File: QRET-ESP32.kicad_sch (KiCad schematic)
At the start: 3 parts

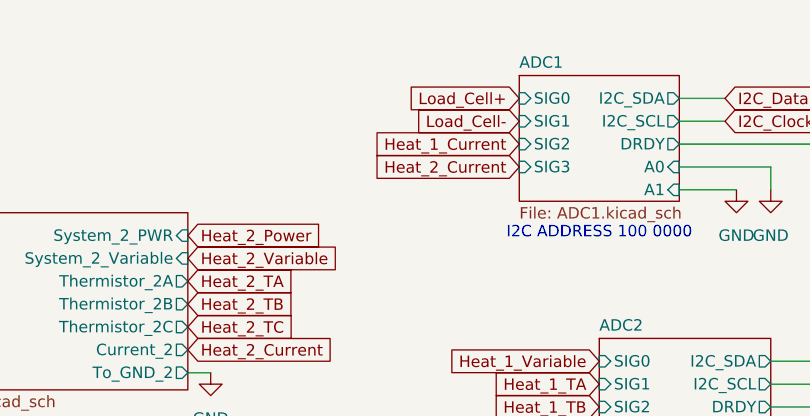
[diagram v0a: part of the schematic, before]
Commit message: Placed the general sets of components.
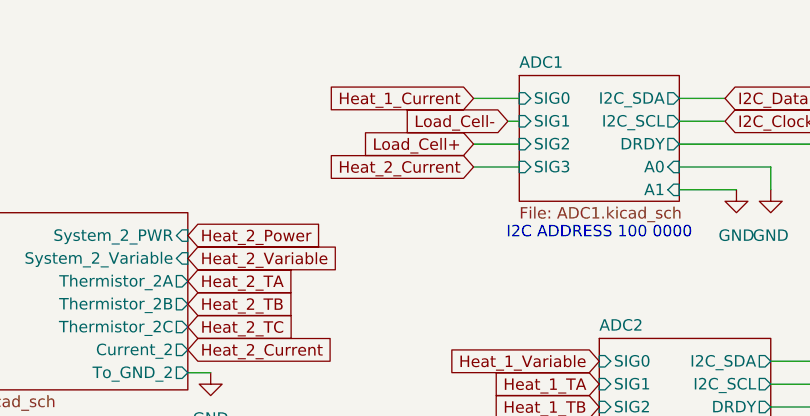
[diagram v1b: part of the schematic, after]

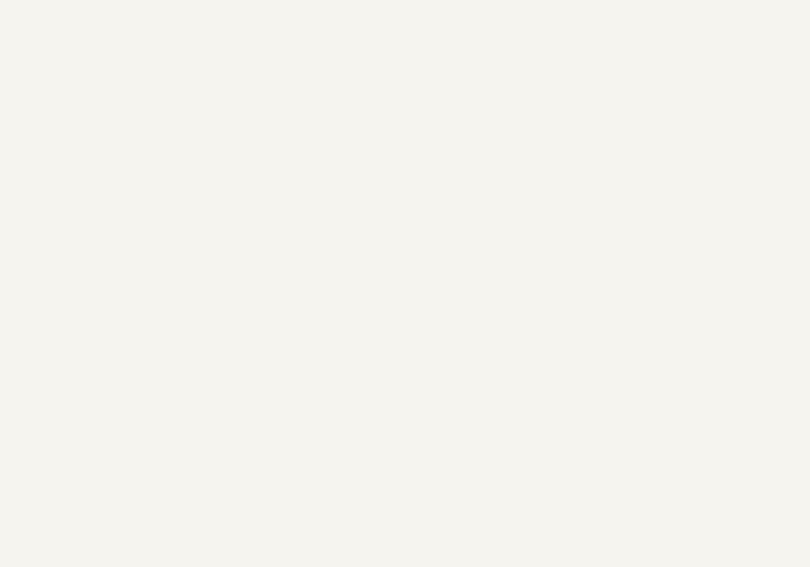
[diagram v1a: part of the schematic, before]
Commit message: General board shape, mounting holes, grounding plates.
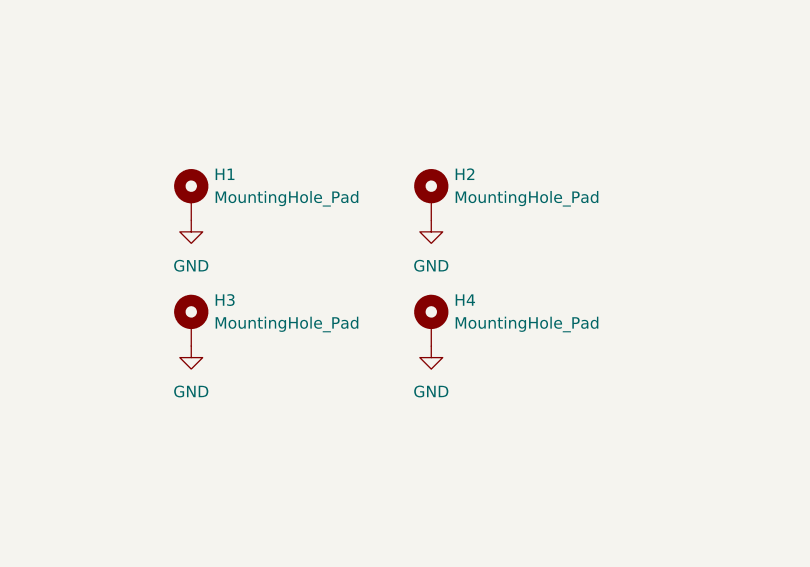
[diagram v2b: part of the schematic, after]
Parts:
- added H1, H2, H3, H4: MountingHole_Pad, MountingHole:MountingHole_3.2mm_M3_ISO7380_Pad, symbol Mechanical:MountingHole_Pad
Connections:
- net GND: now also H1.1, H2.1, H3.1, H4.1

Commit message: Second draft of placement and wiring.
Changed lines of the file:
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@@
+	(wire
+		(pts
+			(xy 129.54 40.64) (xy 129.54 41.91)
+		)
+		(stroke
+			(width 0)
+			(type default)
+		)
+	)
 	(wire
 		(pts
@@
 	(wire
 		(pts
+			(xy 176.53 40.64) (xy 176.53 41.91)
+		)
+		(stroke
+			(width 0)
+			(type default)
+		)
+	)
+	(wire
+		(pts
 			(xy 238.76 66.04) (xy 245.11 66.04)
 		)
@@
 	(wire
 		(pts
+			(xy 129.54 41.91) (xy 132.08 41.91)
+		)
+		(stroke
+			(width 0)
+			(type default)
+		)
+	)
+	(wire
+		(pts
+			(xy 176.53 41.91) (xy 173.99 41.91)
+		)
+		(stroke
+			(width 0)
+			(type default)
+		)
+	)
+	(wire
+		(pts
 			(xy 264.16 81.28) (xy 264.16 82.55)
 		)
@@
 		)
 	)
+	(global_label "Heat_2_Power"
+		(shape input)
+		(at 153.67 25.4 0)
+		(fields_autoplaced yes)
+		(effects
+			(font
+				(size 1.27 1.27)
+			)
+			(justify left)
+		)
+		(property "Intersheetrefs" "${INTERSHEET_REFS}"
+			(at 169.718 25.4 0)
+			(effects
+				(font
+					(size 1.27 1.27)
+				)
+				(justify left)
+				(hide yes)
+			)
+		)
+	)
 	(global_label "Fan_1_Control"
 		(shape input)
@@
 		)
 	)
+	(global_label "Heat_1_Power"
+		(shape input)
+		(at 138.43 27.94 180)
+		(fields_autoplaced yes)
+		(effects
+			(font
+				(size 1.27 1.27)
+			)
+			(justify right)
+		)
+		(property "Intersheetrefs" "${INTERSHEET_REFS}"
+			(at 122.382 27.94 0)
+			(effects
+				(font
+					(size 1.27 1.27)
+				)
+				(justify right)
+				(hide yes)
+			)
+		)
+	)
 	(global_label "Nitrous_Control"
 		(shape input)
@@
 		)
 	)
-	(global_label "Heat_1_Power"
-		(shape input)
-		(at 132.08 41.91 180)
-		(fields_autoplaced yes)
-		(effects
-			(font
-				(size 1.27 1.27)
-			)
-			(justify right)
-		)
-		(property "Intersheetrefs" "${INTERSHEET_REFS}"
-			(at 116.032 41.91 0)
-			(effects
-				(font
-					(size 1.27 1.27)
-				)
-				(justify right)
-				(hide yes)
-			)
-		)
-	)
 	(global_label "DRDY1"
 		(shape input)
@@
 				)
 				(justify right)
-				(hide yes)
-			)
-		)
-	)
-	(global_label "Heat_2_Power"
-		(shape input)
-		(at 173.99 41.91 0)
-		(fields_autoplaced yes)
-		(effects
-			(font
-				(size 1.27 1.27)
-			)
-			(justify left)
-		)
-		(property "Intersheetrefs" "${INTERSHEET_REFS}"
-			(at 190.038 41.91 0)
-			(effects
-				(font
-					(size 1.27 1.27)
-				)
-				(justify left)
 				(hide yes)
 			)
@@
 	)
 	(symbol
+		(lib_id "power:+3.3V")
+		(at 129.54 40.64 0)
+		(unit 1)
+		(exclude_from_sim no)
+		(in_bom yes)
+		(on_board yes)
+		(dnp no)
+		(fields_autoplaced yes)
+		(property "Reference" "#PWR07"
+			(at 129.54 44.45 0)
+			(effects
+				(font
+					(size 1.27 1.27)
+				)
+				(hide yes)
+			)
+		)
+		(property "Value" "+3.3V"
+			(at 129.54 35.56 0)
+			(effects
+				(font
+					(size 1.27 1.27)
+				)
+			)
+		)
+		(property "Footprint" ""
+			(at 129.54 40.64 0)
+			(effects
+				(font
+					(size 1.27 1.27)
+				)
+				(hide yes)
+			)
+		)
+		(property "Datasheet" ""
+			(at 129.54 40.64 0)
+			(effects
+				(font
+					(size 1.27 1.27)
+				)
+				(hide yes)
+			)
+		)
+		(property "Description" "Power symbol creates a global label with name \"+3.3V\""
+			(at 129.54 40.64 0)
+			(effects
+				(font
+					(size 1.27 1.27)
+				)
+				(hide yes)
+			)
+		)
+		(pin "1"
+		)
+		(instances
+			(project ""
+				(path "/24817451-dfe0-4b9a-9d93-7304529c9d58"
+					(reference "#PWR07")
+					(unit 1)
+				)
+			)
+		)
+	)
+	(symbol
 		(lib_id "Device:R_Small_US")
 		(at 264.16 85.09 0)
@@
 					(unit 1)
 				)
+			)
+		)
+	)
+	(symbol
+		(lib_id "power:+3.3V")
+		(at 176.53 40.64 0)
+		(unit 1)
+		(exclude_from_sim no)
+		(in_bom yes)
+		(on_board yes)
+		(dnp no)
+		(fields_autoplaced yes)
+		(property "Reference" "#PWR08"
+			(at 176.53 44.45 0)
+			(effects
+				(font
+					(size 1.27 1.27)
+				)
+				(hide yes)
+			)
+		)
+		(property "Value" "+3.3V"
+			(at 176.53 35.56 0)
+			(effects
+				(font
+					(size 1.27 1.27)
+				)
+			)
+		)
+		(property "Footprint" ""
+			(at 176.53 40.64 0)
+			(effects
+				(font
+					(size 1.27 1.27)
+				)
+				(hide yes)
+			)
+		)
+		(property "Datasheet" ""
+			(at 176.53 40.64 0)
+			(effects
+				(font
+					(size 1.27 1.27)
+				)
+				(hide yes)
+			)
+		)
+		(property "Description" "Power symbol creates a global label with name \"+3.3V\""
+			(at 176.53 40.64 0)
+			(effects
+				(font
+					(size 1.27 1.27)
+				)
+				(hide yes)
+			)
+		)
+		(pin "1"
+		)
+		(instances
+			(project ""
+				(path "/24817451-dfe0-4b9a-9d93-7304529c9d58"
+					(reference "#PWR08")
+					(unit 1)
+				)

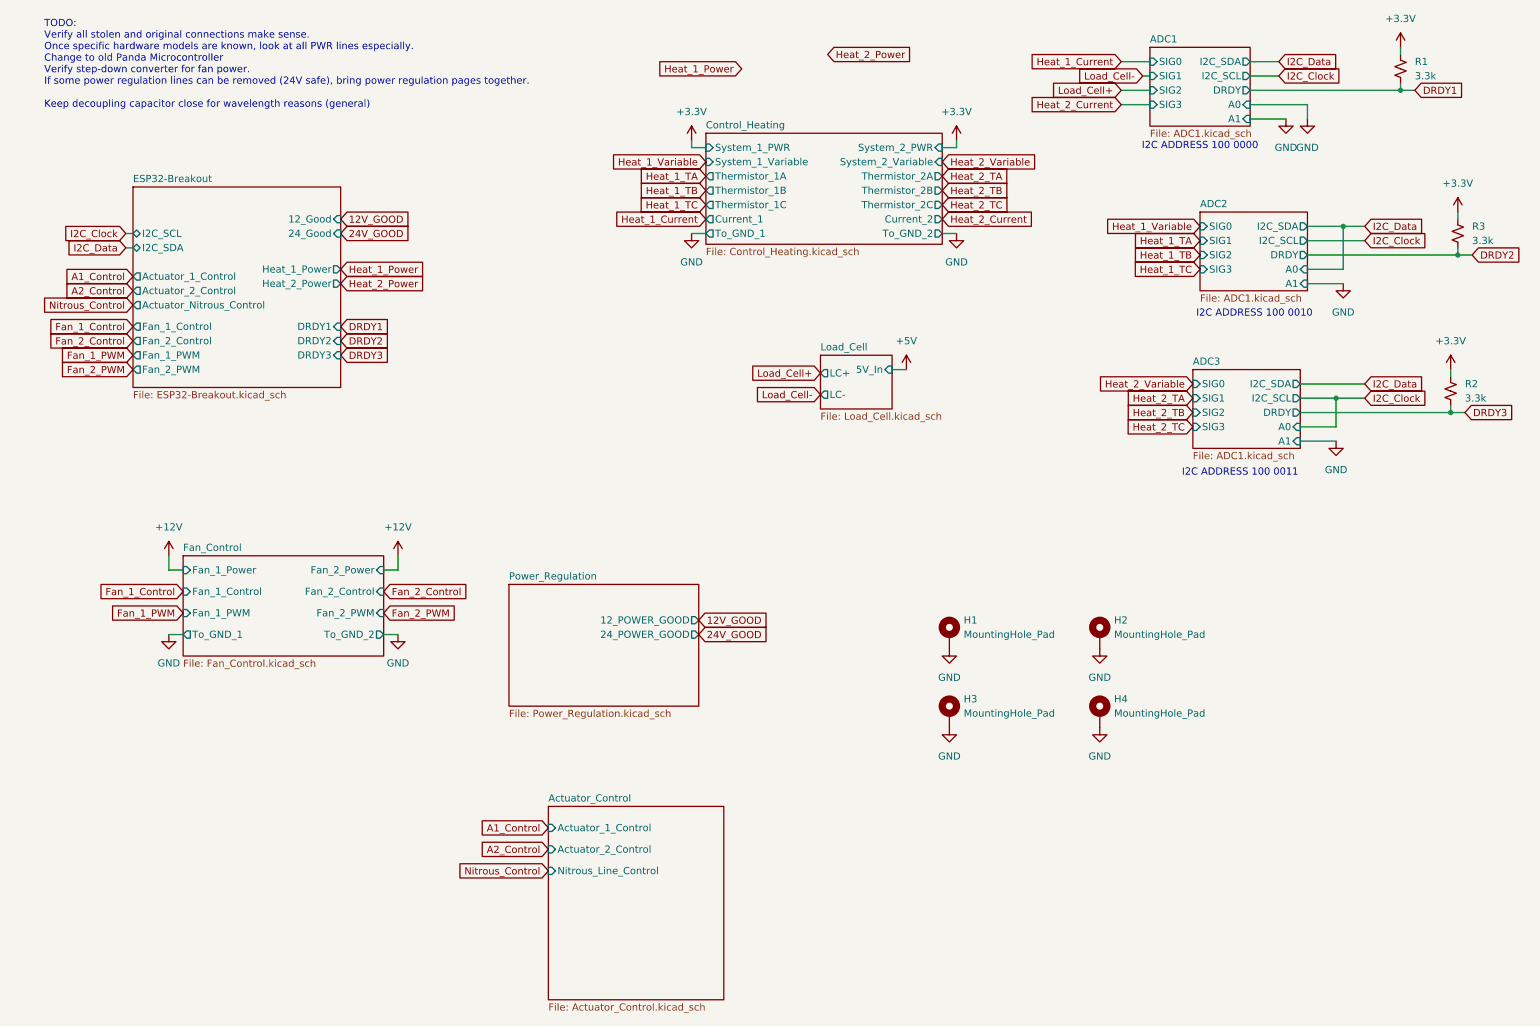
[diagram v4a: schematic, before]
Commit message: remove thermistors from board
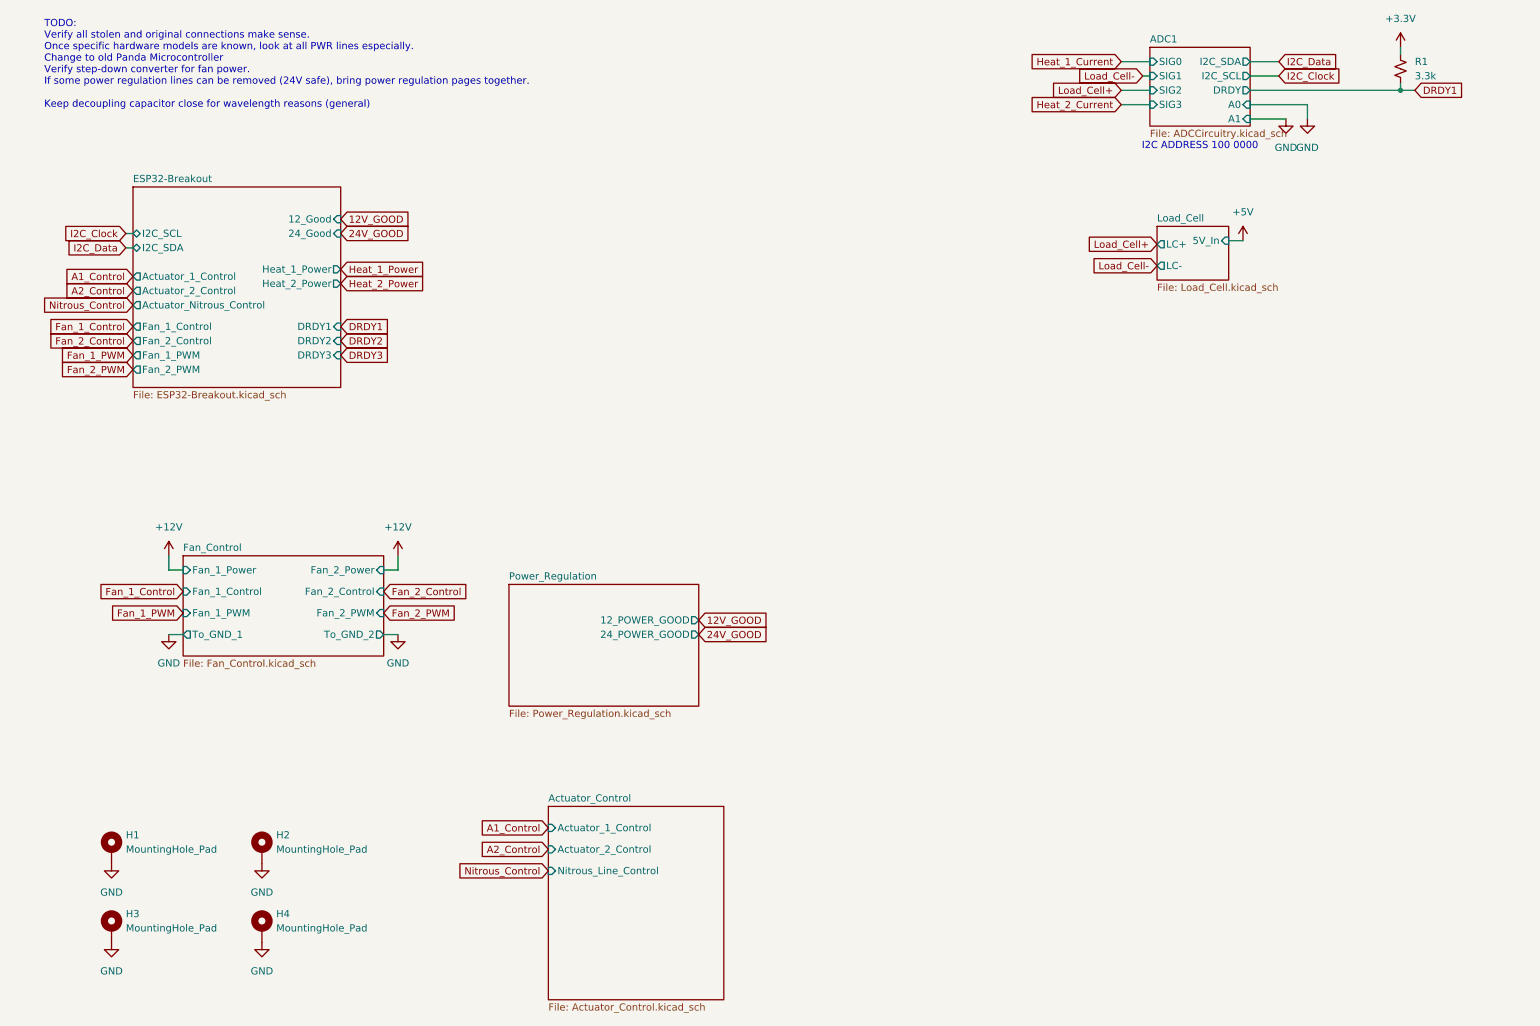
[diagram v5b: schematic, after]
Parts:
- removed R2, R3: 3.3k, Resistor_SMD:R_0402_1005Metric, symbol Device:R_Small_US
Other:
- removed sheet ADC2
- removed sheet ADC3
- removed sheet Control_Heating
- sheet ADC1: file ADC1.kicad_sch -> ADCCircuitry.kicad_sch
- note removed: "I2C ADDRESS 100 0010"
- note removed: "I2C ADDRESS 100 0011"
- moved on the sheet: H1, H2, H3, H4
